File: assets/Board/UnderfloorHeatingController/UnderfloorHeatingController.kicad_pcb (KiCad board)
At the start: 2 copper layers, 54 parts, among them J10 Screw_Terminal_01x02, J11 Screw_Terminal_01x02, J12 Screw_Terminal_01x02, J13 Screw_Terminal_01x02, J14 Screw_Terminal_01x02, J15 Screw_Terminal_01x02, J16 Screw_Terminal_01x02, J2 Screw_Terminal_01x03, J3 Screw_Terminal_01x03, J5 Screw_Terminal_01x02, J6 Screw_Terminal_01x02, J7 Screw_Terminal_01x02, J8 Screw_Terminal_01x02, J9 Screw_Terminal_01x02, K1 G5Q-1A, Q1 BC337, U10 AQY214EH, U11 AQY214EH, U12 AQY214EH, U13 AQY214EH, U14 AQY214EH, U15 AQY214EH, U16 AQY214EH, U2 Waveshare_ESP32-S3-Tiny, U4 AQY214EH, U5 ACS725LLCTR-10AB-T, U6 AQY214EH, U7 AQY214EH, U8 AQY214EH, U9 AQY214EH

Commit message: First complete design.
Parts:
- moved J3 114.7 mm to (113.0, 122.1), turned to 0 degrees
- moved R1 114.5 mm to (106.7, 125.9), turned to 90 degrees
- moved C5 110.4 mm to (109.3, 113.2), turned to 0 degrees
- moved PS1 82.8 mm to (182.2, 91.7)
- moved C3 81.6 mm to (146.8, 89.9)
- moved C2 77.6 mm to (154.9, 115.4)
- moved C4 77.6 mm to (153.7, 110.4)
- moved U5 77.6 mm to (161.3, 111.6)
- moved F1 76.6 mm to (173.9, 114.3), turned to 0 degrees
- moved C1 72.9 mm to (144.3, 82.8), turned to 180 degrees
- moved RV1 69.6 mm to (186.3, 105.3)
- moved J2 66.4 mm to (193.4, 98.0)
- moved R10 65.9 mm to (90.2, 99.1), turned to 180 degrees
- moved K1 63.3 mm to (133.6, 103.6), turned to -90 degrees
- moved J16 62.0 mm to (90.2, 122.1)
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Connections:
- net /SNUB_MOTOR renamed POWER_SNUB_MOTOR
- net Net-(J2-Pin_1) renamed POWER_L_UNFUSED
- RV1 pad 1: POWER_L_MON -> POWER_L
- U2 pad 10: ETA_L1 -> ETA_L2
- U2 pad 11: ETA_L2 -> ETA_L1
- U2 pad 12: ETA_L3 -> ETA_L7
- U2 pad 13: ETA_L4 -> ETA_L8
- U2 pad 14: ETA_L5 -> ETA_L9
- U2 pad 15: ETA_L6 -> ETA_L10
- U2 pad 16: ETA_L7 -> ETA_L11
- U2 pad 17: ETA_L8 -> ETA_L12
- U2 pad 18: ETA_L9 -> unconnected-(U2-15-Pad18)
- U2 pad 19: ETA_L10 -> unconnected-(U2-16-Pad19)
- U2 pad 20: ETA_L11 -> unconnected-(U2-17-Pad20)
- U2 pad 21: ETA_L12 -> unconnected-(U2-18-Pad21)
- U2 pad 6: unconnected-(U2-3-Pad6) -> ETA_L6
- U2 pad 7: unconnected-(U2-4-Pad7) -> ETA_L5
- U2 pad 8: unconnected-(U2-5-Pad8) -> ETA_L4
- U2 pad 9: unconnected-(U2-6-Pad9) -> ETA_L3
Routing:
- net POWER_N: track 0.00 -> 356.0 mm
- net POWER_L_MON: track 0.00 -> 295.6 mm, vias 0 -> 4
- net POWER_PE: track 0.00 -> 109.6 mm, vias 0 -> 1
- net ETA_L1: track 0.00 -> 89.7 mm
- net ETA_L7: track 0.00 -> 80.0 mm
- net ETA_L2: track 0.00 -> 78.5 mm
- net ETA_L3: track 0.00 -> 68.5 mm
- net MOTOR_CTRL: track 0.00 -> 67.4 mm, vias 0 -> 2
- net CURRENT_MON: track 0.00 -> 67.3 mm, vias 0 -> 2
- net +3V3: track 0.00 -> 66.6 mm, vias 0 -> 2
- net ETA_L8: track 0.00 -> 66.4 mm
- net ETA_L4: track 0.00 -> 63.0 mm
- net ETA_L5: track 0.00 -> 54.0 mm
- net +5V: track 0.00 -> 51.2 mm
- net ETA_L9: track 0.00 -> 51.1 mm
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- added copper zone on B.Cu, net GND
- added copper zone on F.Cu, net GND
- added copper zone on F.Cu, net POWER_L
- added copper zone on F.Cu, net POWER_L_MON
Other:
- board outline added: 172.7 x 52.3 mm

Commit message: Minor tweaks.
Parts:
- added R4: 100, Resistor_SMD:R_0805_2012Metric_Pad1.20x1.40mm_HandSolder, F.Cu at (173.4, 102.7)
- moved C2 25.6 mm to (178.1, 104.6)
- moved C4 24.4 mm to (175.2, 98.9)
- moved R15 23.2 mm to (104.3, 95.7)
- moved C5 23.2 mm to (129.8, 102.2)
- moved J8 23.2 mm to (92.8, 72.6)
- moved R13 23.2 mm to (81.4, 95.7)
- moved U14 23.2 mm to (89.0, 95.7)
- moved U16 23.2 mm to (111.9, 95.7)
- moved J12 23.2 mm to (64.9, 111.1)
- moved J5 23.2 mm to (58.6, 72.6)
- moved J6 23.2 mm to (70.0, 72.6)
- moved R5 23.2 mm to (53.5, 88.1)
- moved R7 23.2 mm to (76.3, 88.1)
- moved U12 23.2 mm to (66.2, 95.7)
- moved U4 23.2 mm to (57.3, 88.1)
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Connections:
- U5 pad 7: CURRENT_MON -> Net-(U5-VIOUT)
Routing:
- net Net-(U5-VIOUT): track 0.00 -> 5.47 mm
- net POWER_N: track 356.0 -> 359.2 mm
- net POWER_L_MON: track 295.6 -> 297.3 mm, vias 4 -> 6
- net Net-(U5-FILTER): track 5.31 -> 4.17 mm
- net +3V3: track 66.6 -> 65.8 mm
- net CURRENT_MON: track 67.3 -> 66.7 mm
- net GND: vias 33 -> 36
- net POWER_L: vias 3 -> 5
- added copper zone on B.Cu, net POWER_L
- added copper zone on B.Cu, net POWER_L_MON
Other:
- board size 172.7 x 52.3 mm -> 173.7 x 52.3 mm

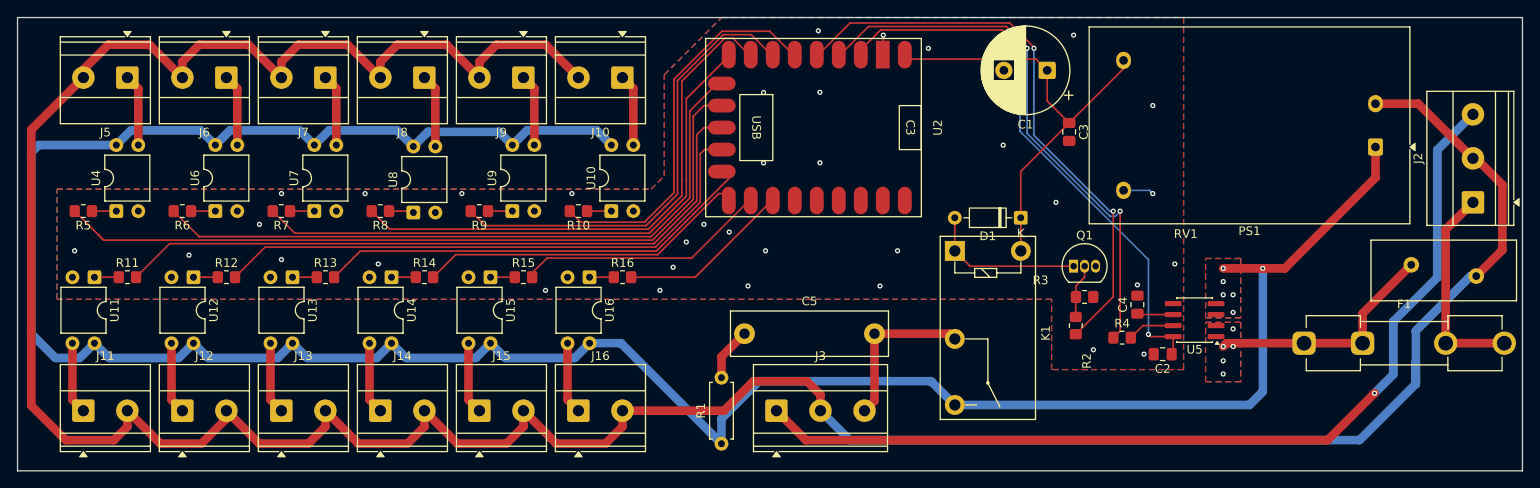
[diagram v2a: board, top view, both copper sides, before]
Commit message: Created space for the varistor and cleaned up some of the poors.
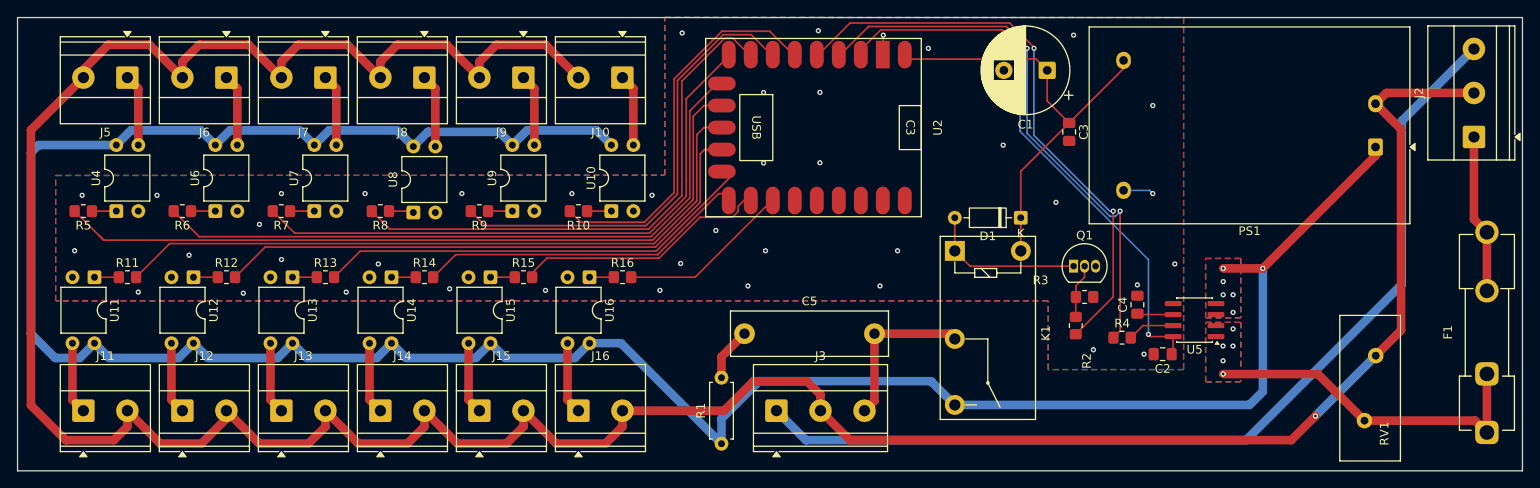
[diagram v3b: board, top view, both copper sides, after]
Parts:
- RV1: footprint Varistor:RV_Disc_D16.5mm_W6.7mm_P7.5mm -> Custom Footprints:RV_Disc_D16.5mm_W6.7mm_P7.5mm with courtyard
- moved F1 23.5 mm to (215.5, 113.6), turned to 90 degrees
- moved RV1 18.8 mm to (201.4, 112.2), turned to 90 degrees
- moved J2 7.55 mm to (214.0, 79.5)
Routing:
- net POWER_L: track 27.6 -> 40.0 mm
- net POWER_N: track 359.2 -> 350.8 mm, vias 0 -> 1
- net POWER_L_UNFUSED: track 24.3 -> 18.4 mm
- net POWER_PE: track 109.6 -> 111.7 mm, vias 1 -> 0
- net POWER_L_MON: track 297.3 -> 295.9 mm
- net ETA_L11: track 29.9 -> 30.5 mm
- net GND: vias 36 -> 42

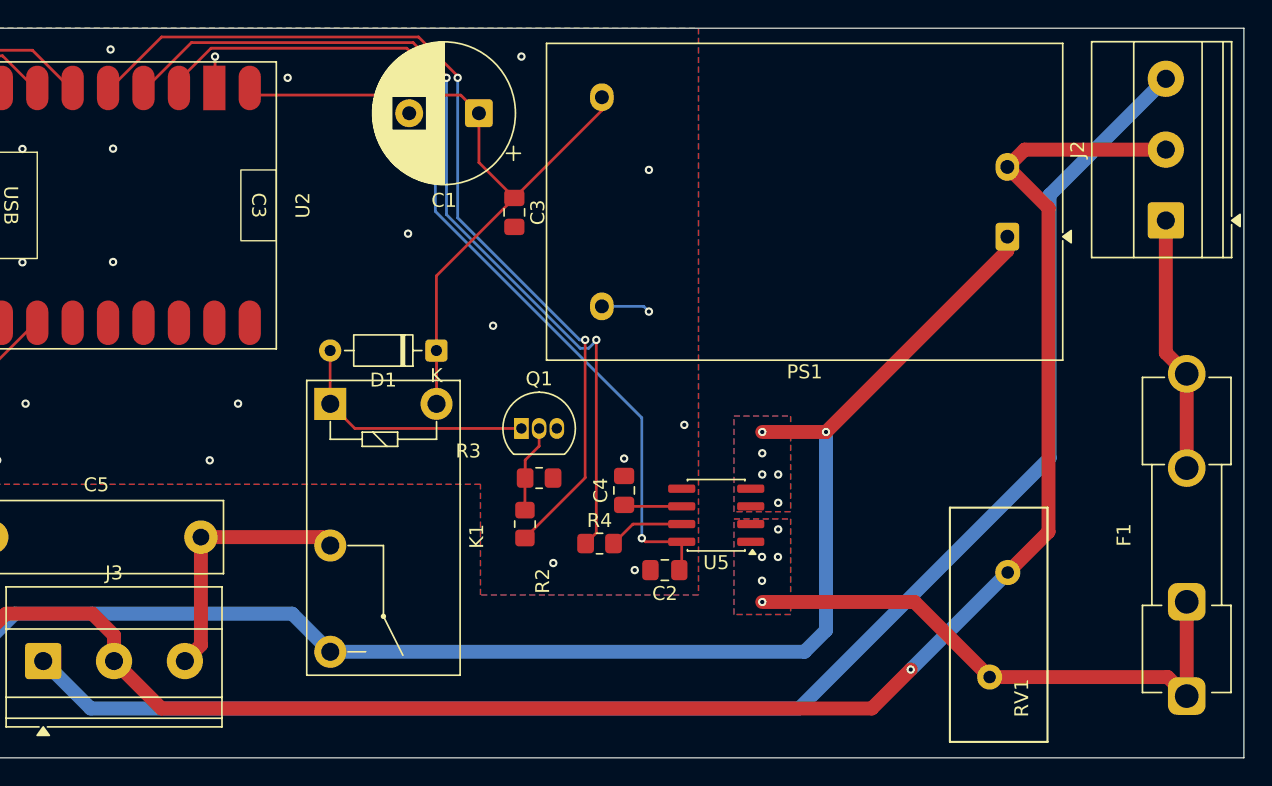
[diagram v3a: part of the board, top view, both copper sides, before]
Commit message: Rerouted HV.
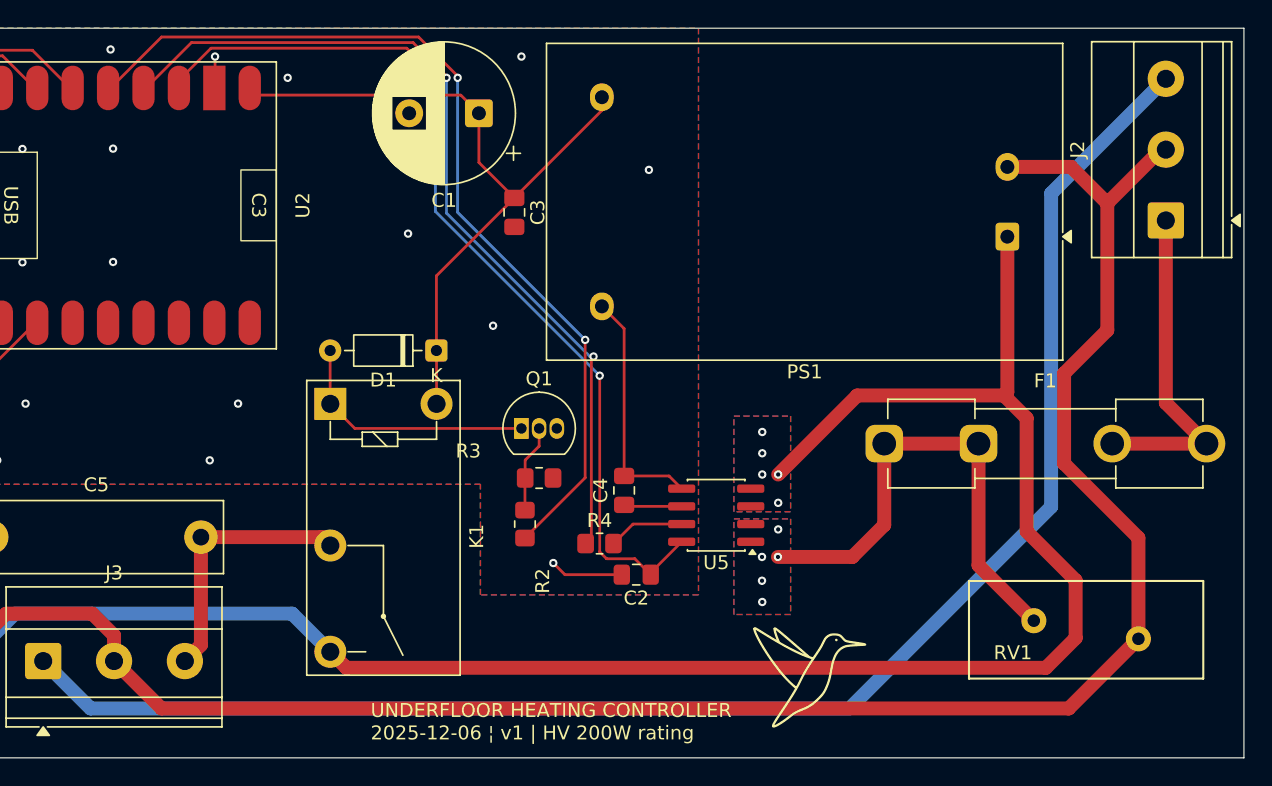
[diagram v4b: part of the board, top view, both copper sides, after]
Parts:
- added G***: LOGO, Custom Footprints:Eletronica Logo, F.Cu at (188.5, 112.3)
- moved F1 28.3 mm to (193.8, 95.5), turned to 0 degrees
- moved RV1 5.14 mm to (204.5, 108.2), turned to 0 degrees
- moved C2 2.08 mm to (176.0, 104.9)
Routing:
- net POWER_L_MON: track 295.9 -> 325.9 mm, vias 6 -> 5
- net GND: track 6.60 -> 25.7 mm, vias 42 -> 38
- net POWER_N: track 350.8 -> 363.6 mm, vias 1 -> 0
- net POWER_L_UNFUSED: track 18.4 -> 24.0 mm
- net POWER_L: track 40.0 -> 35.5 mm
- net +3V3: track 65.8 -> 68.1 mm
- net POWER_PE: track 111.7 -> 113.8 mm
- net CURRENT_MON: track 66.7 -> 65.1 mm
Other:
- board text added: "UNDERFLOOR HEATING CONTROLLER 2025-12-06 ¦ v1 | HV 200W rating"
